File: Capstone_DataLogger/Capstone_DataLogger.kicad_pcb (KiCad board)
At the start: 2 copper layers, 28 parts, among them J1 S2B-PH-K-SLFSN, J10 RJ9, J2 MSD-4-A, J3 S5B-PH-K-S, J7 S4B-PH-K-SLFSN, J8 S4B-PH-K-SLFSN, J9 S4B-PH-K-SLFSN, Q1 NMOS, U1 ESP32-WROOM-32U, U3 ATmega328-P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

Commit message: basic changes
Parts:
- moved U1 69.3 mm to (132.9, 54.0)
- moved J2 40.5 mm to (147.3, 129.5)
- moved J8 36.6 mm to (174.3, 139.7)
- moved U7 20.8 mm to (160.0, 111.8)
- moved J10 19.6 mm to (122.1, 120.1)
- moved J9 19.6 mm to (173.3, 127.0)
- moved XTAL1 12.2 mm to (193.1, 86.4)
- moved Y2 12.0 mm to (151.1, 58.4)
- moved U6 10.2 mm to (137.2, 114.3)
- moved U4 9.86 mm to (157.5, 50.8)
- moved J3 9.13 mm to (159.6, 68.6)
- moved U3 4.38 mm to (172.7, 45.7)
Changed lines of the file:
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@@
 	(footprint "Capstone:CONN_S5B-PH-K-S_JST"
 		(layer "F.Cu")
-		(at 153.3313 75.175)
+		(at 159.640001 68.58)
 		(tags "S5B-PH-K-S ")
 		(property "Reference" "J3"
@@
 	(footprint "Package_DIP:DIP-28_W7.62mm"
 		(layer "F.Cu")
-		(at 177.038 44.958)
+		(at 172.72 45.72)
 		(descr "28-lead though-hole mounted DIP package, row spacing 7.62 mm (300 mils)")
 		(tags "THT DIP DIL PDIP 2.54mm 7.62mm 300mil")
@@
 	(footprint "Capstone:CUI_MSD-4-A"
 		(layer "F.Cu")
-		(at 119.792 99.83 -90)
+		(at 147.32 129.54 -90)
 		(property "Reference" "J2"
 			(at -4.325 -11.135 90)
@@
 	(footprint "Capstone:Cylindrical Can, Radial"
 		(layer "F.Cu")
-		(at 161.637 64.3004)
+		(at 151.13 58.42)
 		(property "Reference" "Y2"
-			(at 0 -0.5 0)
+			(at 0 0 0)
 			(unlocked yes)
 			(layer "F.SilkS")
@@
 	(footprint "Capstone:XTAL_PS1240P02BT_TDK"
 		(layer "F.Cu")
-		(at 184.738 95.25)
+		(at 193.12 86.36)
 		(tags "PS1240P02BT ")
 		(property "Reference" "XTAL1"
@@
 	(footprint "Capstone:CONN_S4B-PH-K-S_JST"
 		(layer "F.Cu")
-		(at 180.222901 145.3026)
+		(at 173.260001 127)
 		(tags "S4B-PH-K-SLFSN ")
 		(property "Reference" "J9"
@@
 	(footprint "Capstone:PDIP8_300MC_MCH"
 		(layer "F.Cu")
-		(at 149.9145 57.1252)
+		(at 157.48 50.8)
 		(tags "MCP7940M-I/P ")
 		(property "Reference" "U4"
@@
 	(footprint "Connector_RJ:RJ9_Evercom_5301-440xxx_Horizontal"
 		(layer "F.Cu")
-		(at 122.428 139.7 -90)
+		(at 122.09 120.08 -90)
 		(descr "Evercom 5301-4P4C RJ9 receptacle, unshielded, https://datasheet.lcsc.com/lcsc/2207051802_EVERCOM-5301-4P4C_C3097715.pdf")
 		(tags "RJ9 Connector tab down")
@@
 	(footprint "Capstone:CONN_S4B-PH-K-S_JST"
 		(layer "F.Cu")
-		(at 141.360901 155.4626)
+		(at 174.340002 139.7)
 		(tags "S4B-PH-K-SLFSN ")
 		(property "Reference" "J8"
@@
 	(footprint "Capstone:N16"
 		(layer "F.Cu")
-		(at 147.32 113.538)
+		(at 137.16 114.3)
 		(tags "CD74HC4050E ")
 		(property "Reference" "U6"
@@
 	(footprint "RF_Module:ESP32-WROOM-32U"
 		(layer "F.Cu")
-		(at 121.724 122.328 90)
+		(at 132.89 53.975 90)
 		(descr "Single 2.4 GHz Wi-Fi and Bluetooth combo chip with U.FL connector, https://www.espressif.com/sites/default/files/documentation/esp32-wroom-32d_esp32-wroom-32u_datasheet_en.pdf")
 		(tags "Single 2.4 GHz Wi-Fi and Bluetooth combo  chip")
@@
 	(footprint "Capstone:N14"
 		(layer "F.Cu")
-		(at 159.258 132.588)
+		(at 160.02 111.76)
 		(tags "SN74HC08N ")
 		(property "Reference" "U7"

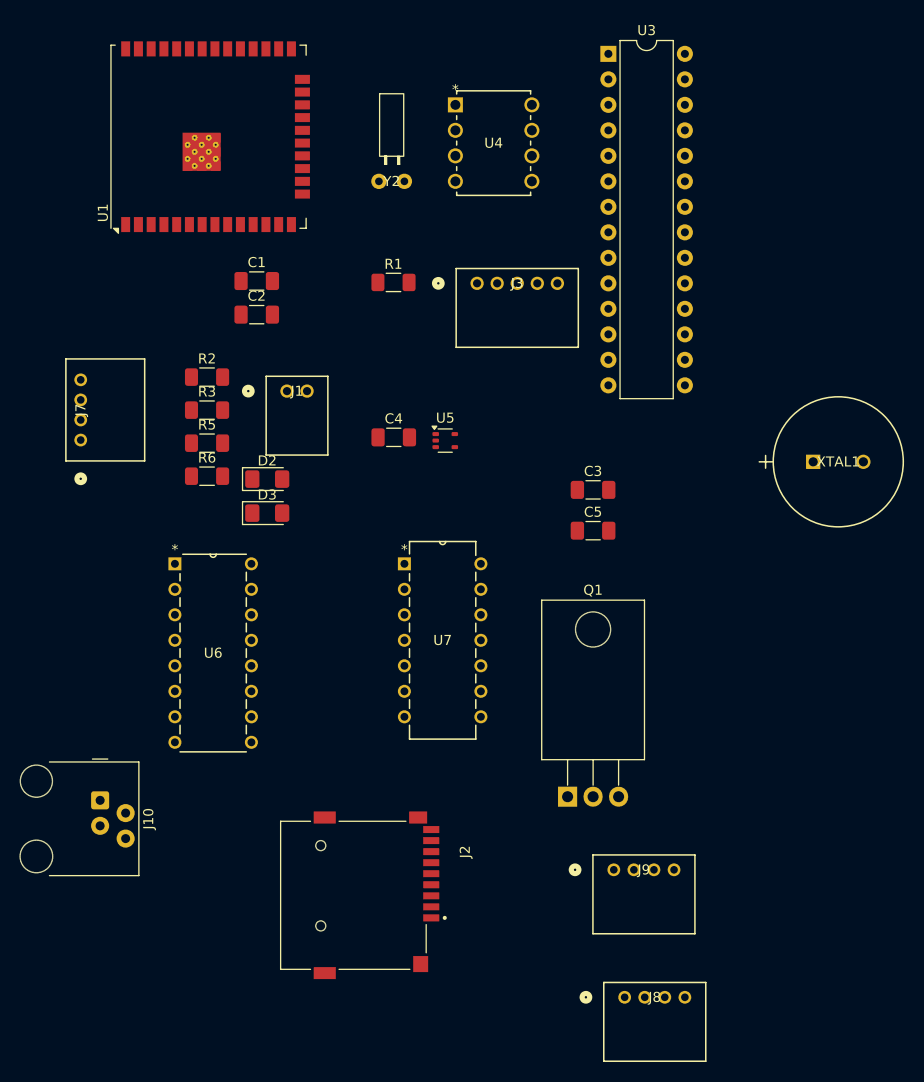
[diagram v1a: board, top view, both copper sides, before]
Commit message: pcb componet placement changed
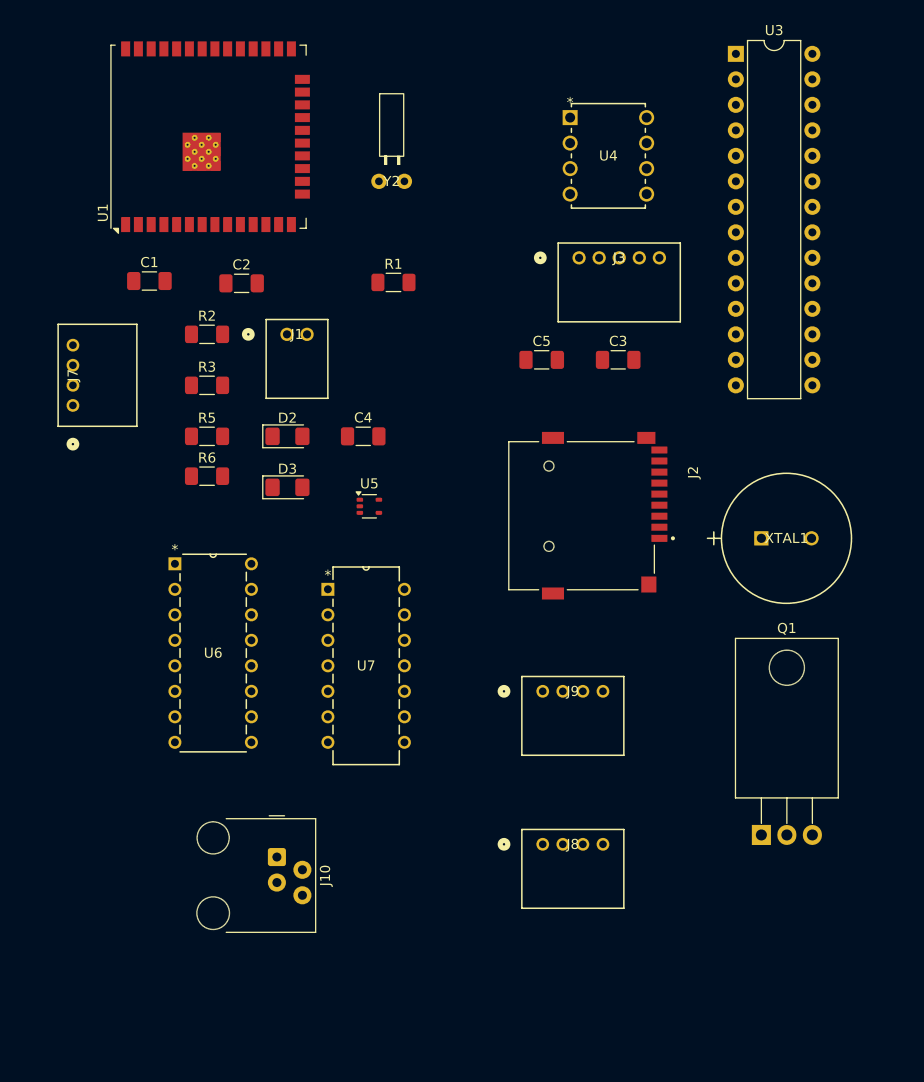
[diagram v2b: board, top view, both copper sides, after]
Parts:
- moved J2 44.1 mm to (170.1, 91.7)
- moved Q1 19.7 mm to (188.0, 123.5)
- moved J9 19.1 mm to (166.2, 109.2)
- moved J10 18.5 mm to (139.7, 125.7)
- moved C5 17.8 mm to (166.1, 76.2)
- moved J8 17.3 mm to (166.2, 124.5)
- moved C3 13.2 mm to (173.7, 76.2)
- moved U3 12.7 mm to (185.4, 45.7)
- moved U4 11.5 mm to (168.9, 52.1)
- moved C1 10.7 mm to (127.0, 68.3)
- moved J3 10.5 mm to (169.8, 66.0)
- moved U5 10.00 mm to (148.9, 90.8)
- moved XTAL1 9.20 mm to (188.0, 94.0)
- moved U7 8.03 mm to (152.4, 114.3)
- moved J1 5.66 mm to (140.7, 73.7)
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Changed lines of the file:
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@@
 	(footprint "Diode_SMD:D_1206_3216Metric_Pad1.42x1.75mm_HandSolder"
 		(layer "F.Cu")
-		(at 138.735 88.08)
+		(at 140.7525 83.82)
 		(descr "Diode SMD 1206 (3216 Metric), square (rectangular) end terminal, IPC_7351 nominal, (Body size source: http://www.tortai-tech.com/upload/download/2011102023233369053.pdf), generated with kicad-footprint-generator")
 		(tags "diode handsolder")
@@
 	(footprint "Package_TO_SOT_THT:TO-220-3_Horizontal_TabDown"
 		(layer "F.Cu")
-		(at 168.656 119.72)
+		(at 187.96 123.53)
 		(descr "TO-220-3, Horizontal, RM 2.54mm, see https://www.vishay.com/docs/66542/to-220-1.pdf")
 		(tags "TO-220-3 Horizontal RM 2.54mm")
@@
 	(footprint "Resistor_SMD:R_1206_3216Metric_Pad1.30x1.75mm_HandSolder"
 		(layer "F.Cu")
-		(at 132.74 81.21)
+		(at 132.74 78.74)
 		(descr "Resistor SMD 1206 (3216 Metric), square (rectangular) end terminal, IPC_7351 nominal with elongated pad for handsoldering. (Body size source: IPC-SM-782 page 72, https://www.pcb-3d.com/wordpress/wp-content/uploads/ipc-sm-782a_amendment_1_and_2.pdf), generated with kicad-footprint-generator")
 		(tags "resistor handsolder")
@@
 	(footprint "Capstone:CONN_S4B-PH-K-S_JST"
 		(layer "F.Cu")
-		(at 120.1566 84.191099 90)
+		(at 119.38 80.739999 90)
 		(tags "S4B-PH-K-SLFSN ")
 		(property "Reference" "J7"
@@
 	(footprint "Resistor_SMD:R_1206_3216Metric_Pad1.30x1.75mm_HandSolder"
 		(layer "F.Cu")
-		(at 132.74 77.92)
+		(at 132.74 73.66)
 		(descr "Resistor SMD 1206 (3216 Metric), square (rectangular) end terminal, IPC_7351 nominal with elongated pad for handsoldering. (Body size source: IPC-SM-782 page 72, https://www.pcb-3d.com/wordpress/wp-content/uploads/ipc-sm-782a_amendment_1_and_2.pdf), generated with kicad-footprint-generator")
 		(tags "resistor handsolder")
@@
 	(footprint "Package_TO_SOT_SMD:SOT-353_SC-70-5"
 		(layer "F.Cu")
-		(at 156.47 84.245)
+		(at 148.91 90.79)
 		(descr "SOT-353, SC-70-5")
 		(tags "SOT-353 SC-70-5")
@@
 	(footprint "Capstone:CONN_S5B-PH-K-S_JST"
 		(layer "F.Cu")
-		(at 159.640001 68.58)
+		(at 169.800001 66.04)
 		(tags "S5B-PH-K-S ")
 		(property "Reference" "J3"
@@
 	(footprint "Package_DIP:DIP-28_W7.62mm"
 		(layer "F.Cu")
-		(at 172.72 45.72)
+		(at 185.42 45.72)
 		(descr "28-lead though-hole mounted DIP package, row spacing 7.62 mm (300 mils)")
 		(tags "THT DIP DIL PDIP 2.54mm 7.62mm 300mil")
@@
 	(footprint "Capstone:CUI_MSD-4-A"
 		(layer "F.Cu")
-		(at 147.32 129.54 -90)
+		(at 170.05 91.73 -90)
 		(property "Reference" "J2"
 			(at -4.325 -11.135 90)
@@
 	(footprint "Diode_SMD:D_1206_3216Metric_Pad1.42x1.75mm_HandSolder"
 		(layer "F.Cu")
-		(at 138.735 91.47)
+		(at 140.7525 88.9)
 		(descr "Diode SMD 1206 (3216 Metric), square (rectangular) end terminal, IPC_7351 nominal, (Body size source: http://www.tortai-tech.com/upload/download/2011102023233369053.pdf), generated with kicad-footprint-generator")
 		(tags "diode handsolder")
@@
 	(footprint "Capstone:CONN_S2B-PH-K-S_JST"
 		(layer "F.Cu")
-		(at 140.7014 79.315)
+		(at 140.7014 73.66)
 		(tags "S2B-PH-K-SLFSN ")
 		(property "Reference" "J1"
@@
 	(footprint "Capacitor_SMD:C_1206_3216Metric_Pad1.33x1.80mm_HandSolder"
 		(layer "F.Cu")
-		(at 151.34 83.92)
+		(at 148.2975 83.82)
 		(descr "Capacitor SMD 1206 (3216 Metric), square (rectangular) end terminal, IPC_7351 nominal with elongated pad for handsoldering. (Body size source: IPC-SM-782 page 76, https://www.pcb-3d.com/wordpress/wp-content/uploads/ipc-sm-782a_amendment_1_and_2.pdf), generated with kicad-footprint-generator")
 		(tags "capacitor handsolder")
@@
 	(footprint "Capstone:XTAL_PS1240P02BT_TDK"
 		(layer "F.Cu")
-		(at 193.12 86.36)
+		(at 187.96 93.98)
 		(tags "PS1240P02BT ")
 		(property "Reference" "XTAL1"
@@
 	(footprint "Capstone:CONN_S4B-PH-K-S_JST"
 		(layer "F.Cu")
-		(at 173.260001 127)
+		(at 166.18 109.22)
 		(tags "S4B-PH-K-SLFSN ")
 		(property "Reference" "J9"
@@
 	(footprint "Capstone:PDIP8_300MC_MCH"
 		(layer "F.Cu")
-		(at 157.48 50.8)
+		(at 168.91 52.07)
 		(tags "MCP7940M-I/P ")
 		(property "Reference" "U4"
@@
 	(footprint "Connector_RJ:RJ9_Evercom_5301-440xxx_Horizontal"
 		(layer "F.Cu")
-		(at 122.09 120.08 -90)
+		(at 139.7 125.73 -90)
 		(descr "Evercom 5301-4P4C RJ9 receptacle, unshielded, https://datasheet.lcsc.com/lcsc/2207051802_EVERCOM-5301-4P4C_C3097715.pdf")
 		(tags "RJ9 Connector tab down")
@@
 	(footprint "Capacitor_SMD:C_1206_3216Metric_Pad1.33x1.80mm_HandSolder"
 		(layer "F.Cu")
-		(at 137.69 71.7)
+		(at 136.1825 68.58)
 		(descr "Capacitor SMD 1206 (3216 Metric), square (rectangular) end terminal, IPC_7351 nominal with elongated pad for handsoldering. (Body size source: IPC-SM-782 page 76, https://www.pcb-3d.com/wordpress/wp-content/uploads/ipc-sm-782a_amendment_1_and_2.pdf), generated with kicad-footprint-generator")
 		(tags "capacitor handsolder")
@@
 	(footprint "Capstone:CONN_S4B-PH-K-S_JST"
 		(layer "F.Cu")
-		(at 174.340002 139.7)
+		(at 166.18 124.46)
 		(tags "S4B-PH-K-SLFSN ")
 		(property "Reference" "J8"
@@
 	(footprint "Capacitor_SMD:C_1206_3216Metric_Pad1.33x1.80mm_HandSolder"
 		(layer "F.Cu")
-		(at 171.196 89.154)
+		(at 173.6975 76.2)
 		(descr "Capacitor SMD 1206 (3216 Metric), square (rectangular) end terminal, IPC_7351 nominal with elongated pad for handsoldering. (Body size source: IPC-SM-782 page 76, https://www.pcb-3d.com/wordpress/wp-content/uploads/ipc-sm-782a_amendment_1_and_2.pdf), generated with kicad-footprint-generator")
 		(tags "capacitor handsolder")
@@
 	(footprint "Resistor_SMD:R_1206_3216Metric_Pad1.30x1.75mm_HandSolder"
 		(layer "F.Cu")
-		(at 132.74 84.5)
+		(at 132.74 83.82)
 		(descr "Resistor SMD 1206 (3216 Metric), square (rectangular) end terminal, IPC_7351 nominal with elongated pad for handsoldering. (Body size source: IPC-SM-782 page 72, https://www.pcb-3d.com/wordpress/wp-content/uploads/ipc-sm-782a_amendment_1_and_2.pdf), generated with kicad-footprint-generator")
 		(tags "resistor handsolder")
@@
 	(footprint "Capacitor_SMD:C_1206_3216Metric_Pad1.33x1.80mm_HandSolder"
 		(layer "F.Cu")
-		(at 171.196 93.218)
+		(at 166.0775 76.2)
 		(descr "Capacitor SMD 1206 (3216 Metric), square (rectangular) end terminal, IPC_7351 nominal with elongated pad for handsoldering. (Body size source: IPC-SM-782 page 76, https://www.pcb-3d.com/wordpress/wp-content/uploads/ipc-sm-782a_amendment_1_and_2.pdf), generated with kicad-footprint-generator")
 		(tags "capacitor handsolder")
@@
 	(footprint "Capstone:N14"
 		(layer "F.Cu")
-		(at 160.02 111.76)
+		(at 152.4 114.3)
 		(tags "SN74HC08N ")
 		(property "Reference" "U7"
@@
 	(footprint "Capacitor_SMD:C_1206_3216Metric_Pad1.33x1.80mm_HandSolder"
 		(layer "F.Cu")
-		(at 137.69 68.35)
+		(at 127 68.35)
 		(descr "Capacitor SMD 1206 (3216 Metric), square (rectangular) end terminal, IPC_7351 nominal with elongated pad for handsoldering. (Body size source: IPC-SM-782 page 76, https://www.pcb-3d.com/wordpress/wp-content/uploads/ipc-sm-782a_amendment_1_and_2.pdf), generated with kicad-footprint-generator")
 		(tags "capacitor handsolder")

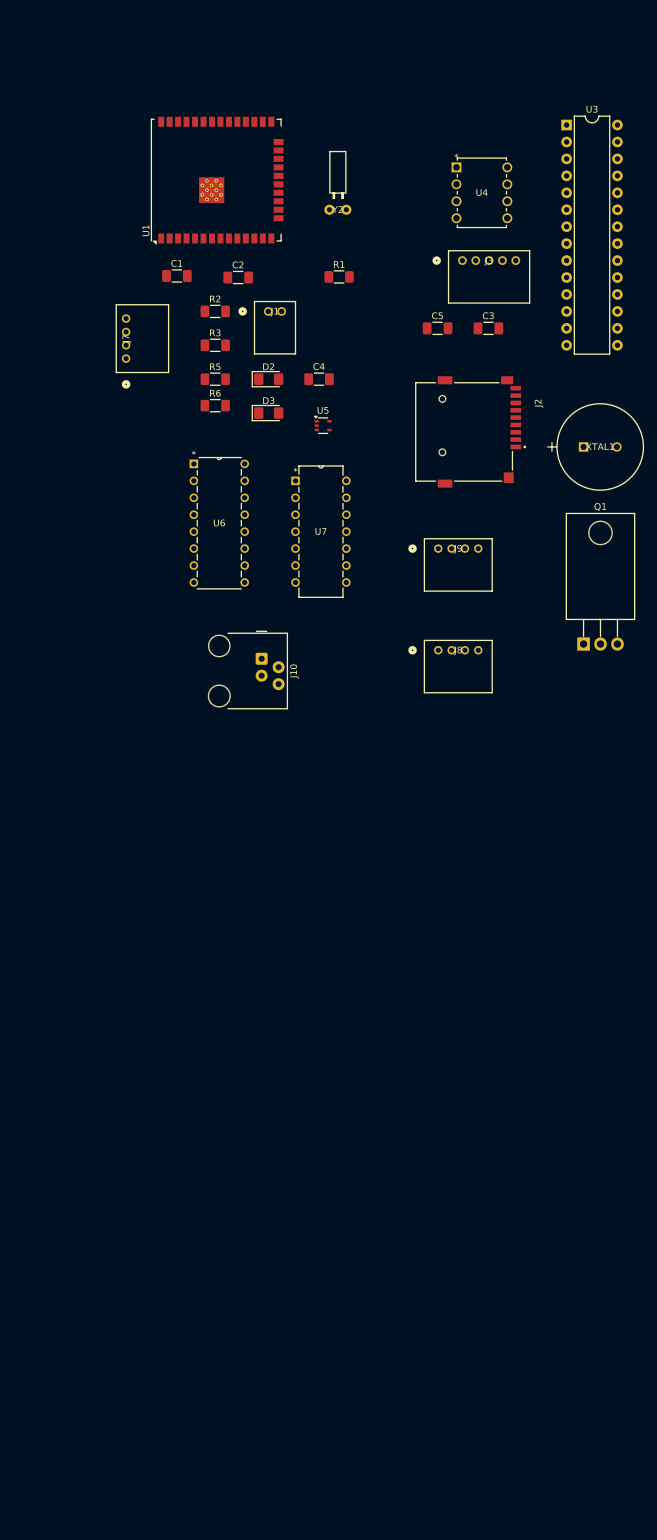
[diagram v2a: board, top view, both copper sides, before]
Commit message: pcb connected except SD card
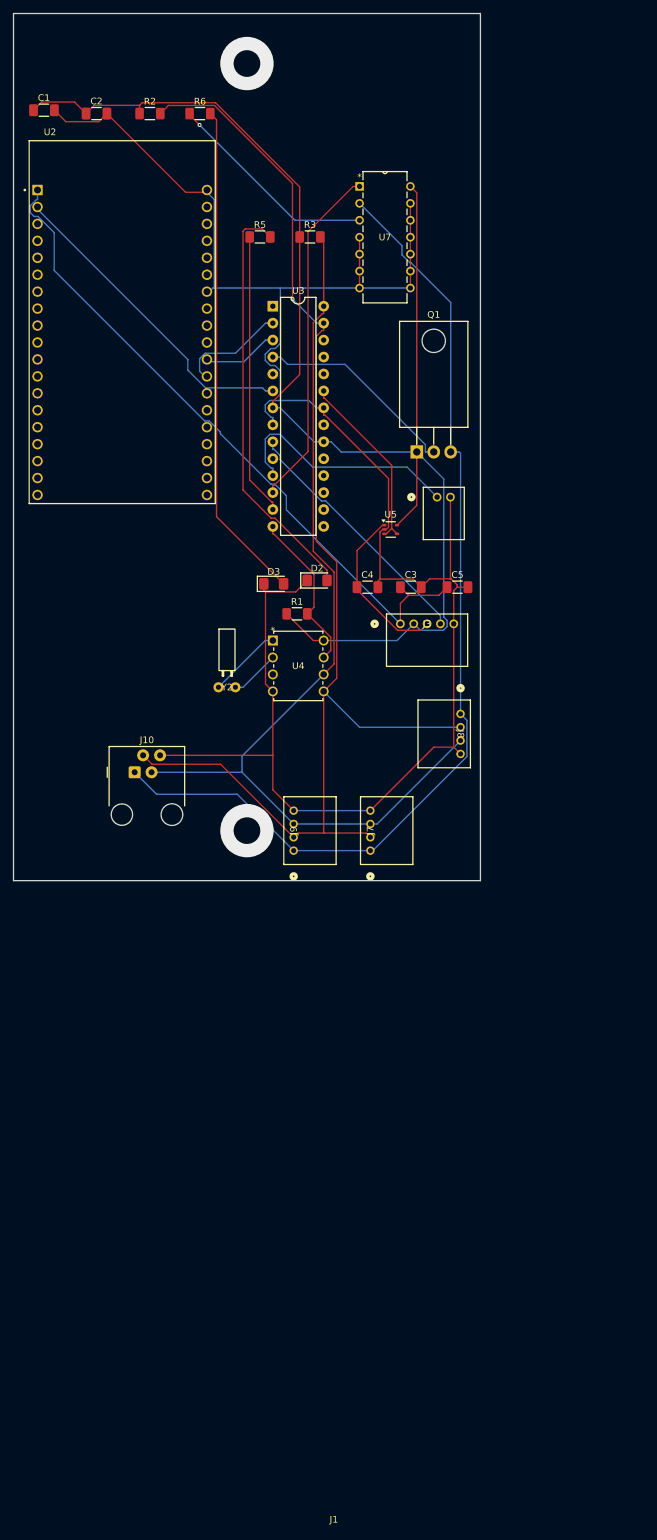
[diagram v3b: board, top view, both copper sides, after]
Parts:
- removed J2: MSD-4-A, Capstone:CUI_MSD-4-A
- removed U1: ESP32-WROOM-32U, RF_Module:ESP32-WROOM-32U
- removed U6: CD74HC4050E, Capstone:N16
- removed XTAL1: PS1240P02BT, Capstone:XTAL_PS1240P02BT_TDK
- added U2: ESP32-DEVKITC-32D, Capstone:MODULE_ESP32-DEVKITC-32D, F.Cu at (118.8, 75.2)
- moved J7 82.4 mm to (156.0, 154.5)
- moved U4 76.1 mm to (141.4, 123.0)
- moved Y2 73.5 mm to (134.5, 130.0)
- moved J3 55.2 mm to (160.5, 120.5)
- moved U3 51.7 mm to (141.4, 72.9)
- moved R1 50.9 mm to (145.0, 119.0)
- moved J9 50.2 mm to (144.5, 154.5), turned to 90 degrees
- moved U7 45.2 mm to (162.0, 70.2)
- moved R6 43.8 mm to (130.4, 44.0)
- moved C3 40.5 mm to (162.1, 115.0)
- moved C5 38.9 mm to (169.1, 115.0)
- moved Q1 38.1 mm to (163.0, 94.7)
- moved J1 37.6 mm to (166.0, 101.5)
- moved C2 32.5 mm to (114.9, 44.0)
- moved C4 32.0 mm to (155.6, 115.0)
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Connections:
- U3 pad 15: /MCU/CD -> unconnected-(U3-PB1-Pad15)
- U3 pad 16: /MCU/CS -> unconnected-(U3-PB2-Pad16)
- U3 pad 17: /MCU/MOSI -> unconnected-(U3-PB3-Pad17)
- U3 pad 18: /MCU/MISO -> unconnected-(U3-PB4-Pad18)
- U3 pad 19: /MCU/CLK -> unconnected-(U3-PB5-Pad19)
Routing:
- net GND: track 0.00 -> 300.1 mm
- net +5V: track 0.00 -> 215.3 mm
- net /MCU/SDA: track 0.00 -> 190.2 mm, vias 0 -> 1
- net +5V_CTRL: track 0.00 -> 150.9 mm, vias 0 -> 1
- net /MCU/SCL: track 0.00 -> 142.9 mm
- net +3.3V: track 0.00 -> 102.1 mm
- net Net-(D3-A): track 0.00 -> 75.1 mm
- net Net-(D2-A): track 0.00 -> 62.7 mm
- net /MCU/IND_1: track 0.00 -> 52.0 mm
- net /MCU/ESP_EN: track 0.00 -> 47.5 mm
- net /MCU/ON_LED: track 0.00 -> 42.4 mm
- net /MCU/PWM_HEATER: track 0.00 -> 38.2 mm
- net Net-(U3-PD5): track 0.00 -> 36.0 mm
- net /MCU/SENSOR_ON_LED: track 0.00 -> 32.2 mm, vias 0 -> 1
- net /MCU/5V_CTRL: track 0.00 -> 30.7 mm
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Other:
- board outline added: 70 x 130 mm

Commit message: pcb connections comeleted
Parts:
- added U1: ~, Connector_Molex:Molex_Micro-Latch_53253-0970_1x09_P2.00mm_Vertical, F.Cu at (123.0, 112.5)
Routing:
- net Net-(U1-CLK): track 0.00 -> 48.8 mm
- net Net-(U1-D2): track 0.00 -> 40.3 mm
- net Net-(U1-D3): track 0.00 -> 37.2 mm
- net +5V: track 215.3 -> 251.0 mm
- net Net-(U1-D1): track 0.00 -> 34.8 mm
- net Net-(U1-CMD): track 0.00 -> 33.2 mm
- net Net-(U1-D0): track 0.00 -> 28.7 mm
- net GND: track 300.1 -> 317.0 mm
- net +5V_CTRL: track 150.9 -> 153.8 mm
- net Net-(U4-X1): track 11.1 -> 12.2 mm
- net /MCU/SCL: track 142.9 -> 143.8 mm
